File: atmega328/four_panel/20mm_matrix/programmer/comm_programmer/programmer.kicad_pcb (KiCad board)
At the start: 2 copper layers, 40 x 40 mm, 3 parts, among them P1 CONN_2, P2 CONN_3X2, P3 CONN15

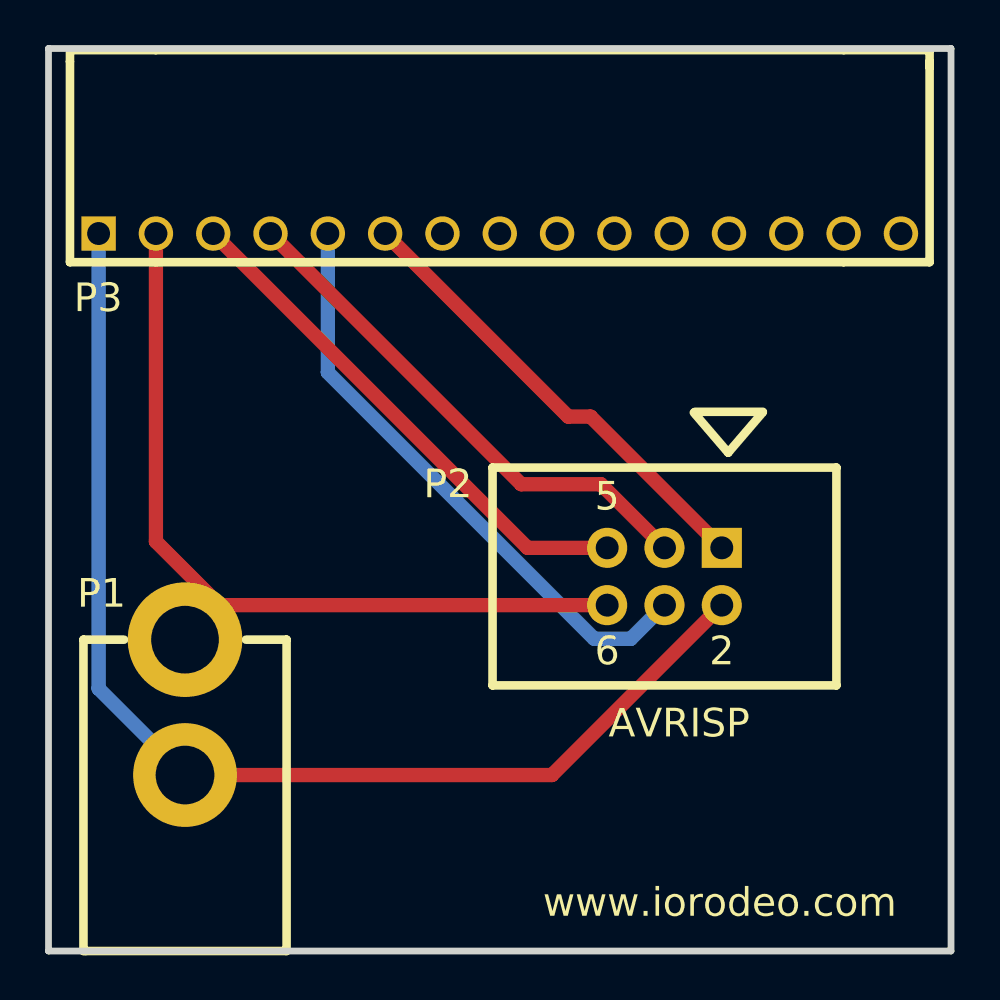
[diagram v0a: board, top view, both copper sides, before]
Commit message: Added bottom pcb for 4x20mm atmega328 panel driver.
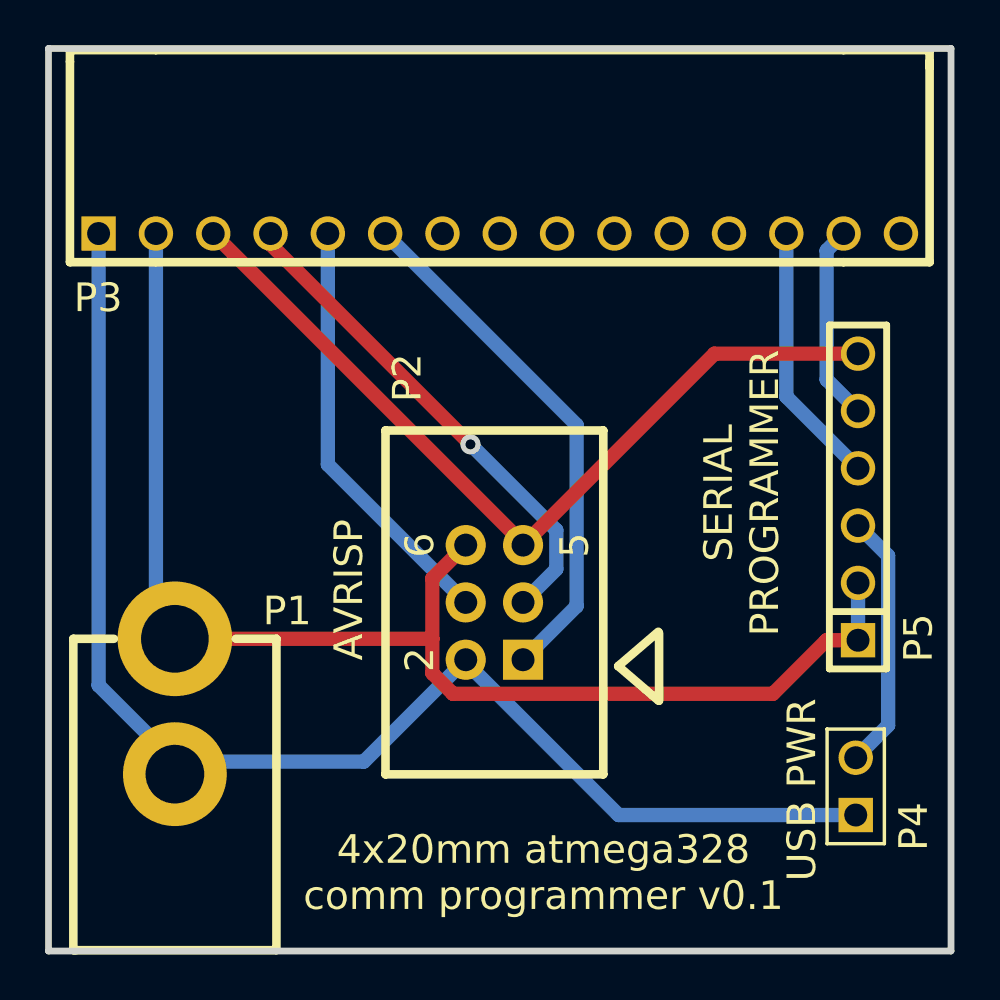
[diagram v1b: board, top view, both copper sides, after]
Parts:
- added P4: CONN_2, PIN_ARRAY_2X1, F.Cu at (85.8, 82.7)
- added P5: CONN_6, PIN_ARRAY-6X1, F.Cu at (85.9, 69.9)
- moved P2 7.63 mm to (69.8, 74.5), turned to 90 degrees
- moved P1 0.45 mm to (55.6, 76.2)
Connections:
- P3 pad 13: N-0000010 (its old number) -> /RX
- P3 pad 14: N-000009 (its old number) -> /TX
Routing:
- net GND: track 37.0 -> 58.8 mm
- net /~RST: track 23.2 -> 37.9 mm
- net /RX: track 0.00 -> 11.7 mm
- net N-0000014: track 0.00 -> 11.4 mm
- net /TX: track 0.00 -> 8.75 mm
- net +5V: track 52.5 -> 60.3 mm
- net /MOSI: track 26.6 -> 18.9 mm
- net /MISO: track 20.7 -> 23.4 mm
- net /SCK: track 23.2 -> 22.2 mm, vias 0 -> 1
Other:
- board text added: "4x20mm atmega328 comm programmer v0.1"
- board text added: "SERIAL PROGRAMMER"
- board text added: "USB PWR"
